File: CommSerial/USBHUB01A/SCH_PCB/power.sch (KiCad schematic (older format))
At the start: 16 parts, among them CON1 PowerIn +5V, J18 JUMP_3X2, SW1 SPST, U3 TPS7A4533KTTR, U4 TPS74801RGWR

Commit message: Vyhozený vypínač, přidaný "Distribution Load Switch"
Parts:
- removed J18: JUMP_3X2, Mlab_Pin_Headers:Straight_2x03, symbol JUMP_3X2
- removed SW1: SPST, Mlab_SW:Prepinaci_3A_SL19121, symbol SPST
- added C1: 10uF, Mlab_R:SMD-0805, symbol C
- added C3: 100nF, Mlab_R:SMD-0603, symbol C
- added D7: LED, Mlab_D:LED_1206, symbol LED
- added R41: 10k, Mlab_R:SMD-0603, symbol R
- added R42: 470R, Mlab_R:SMD-0603, symbol R
- added U9: AP22811, Housings_SSOP:MSOP-8_3x3mm_Pitch0.65mm, symbol AP22811
- C35: value 10uF -> 1uF
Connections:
- net labels added: USB_VBUS_UP
- wire segments 45 -> 61
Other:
- moved on the sheet: C35, C36, C37, C38, C39, C40, D1, R23, R24, R25, R26, U3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

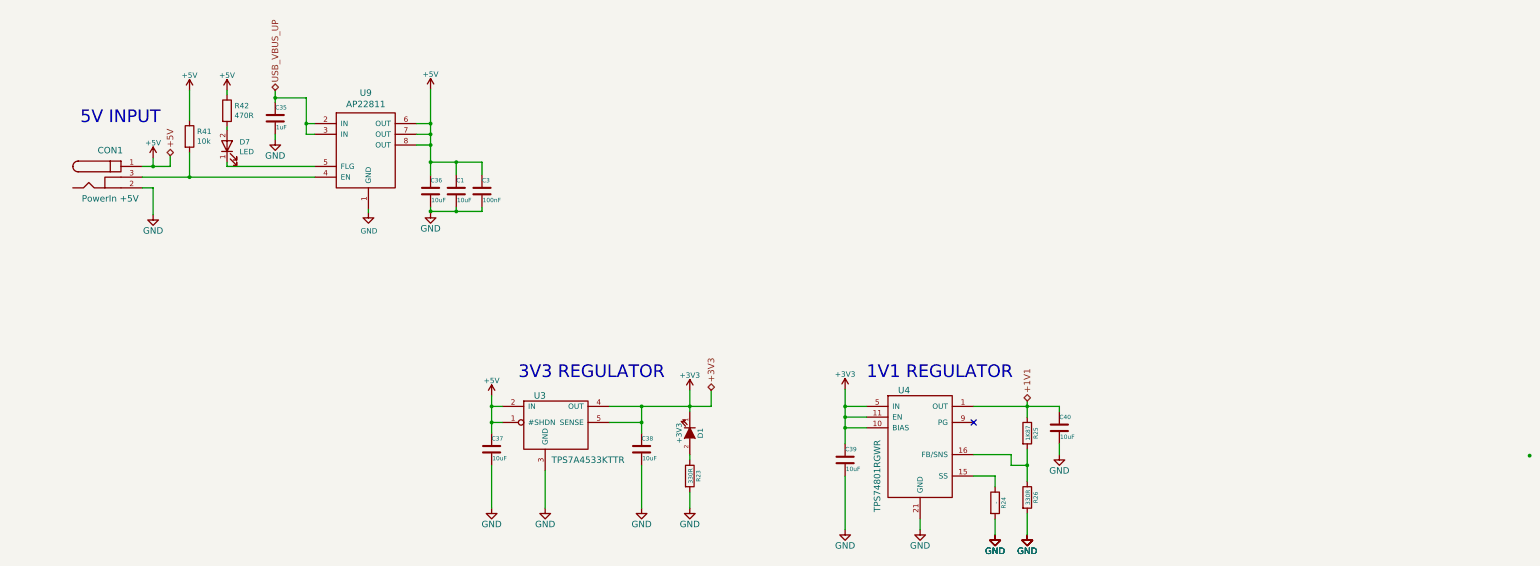
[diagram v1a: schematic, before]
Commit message: Přidání tantalového kondenzátoru na +5V větev
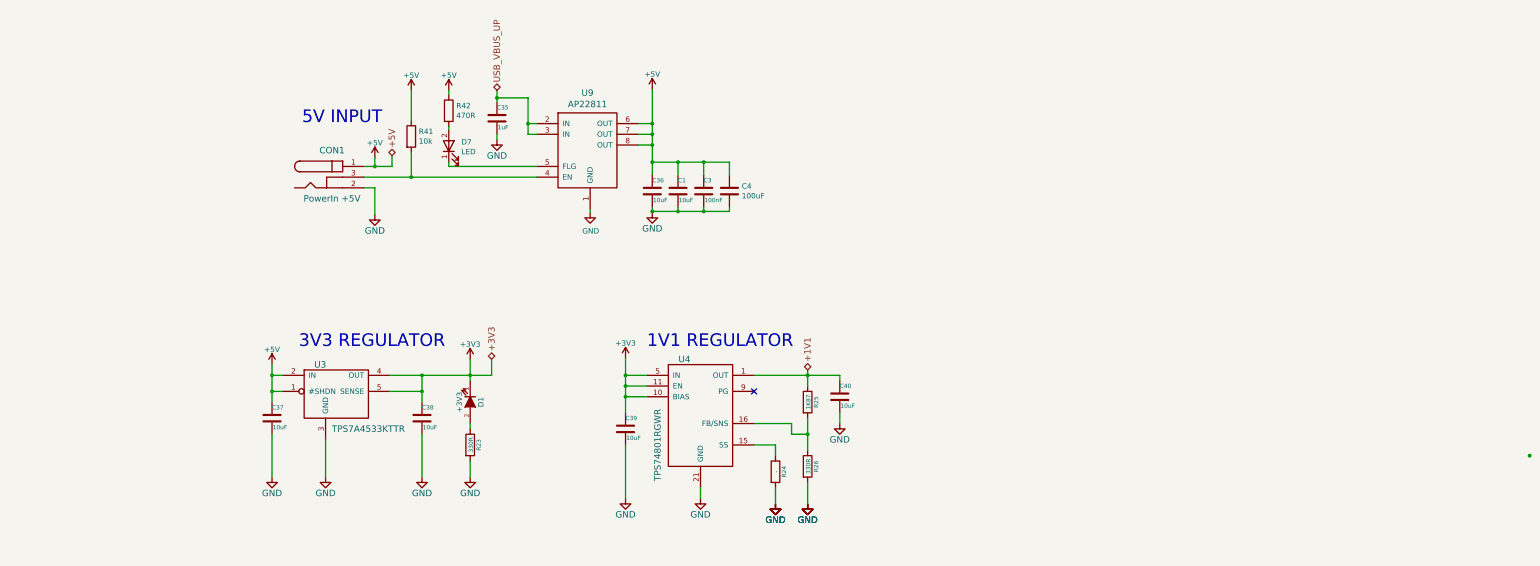
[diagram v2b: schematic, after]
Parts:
- added C4: 100uF, Mlab_C:TantalC_SizeD_Reflow, symbol C
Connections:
- net +5V: now also C4.1
- net GND: now also C4.2
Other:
- moved on the sheet: C1, C3, C35, C36, C37, C38, C39, C40, CON1, D1, D7, R23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

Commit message: USB-Hub-funkcni finalni verze
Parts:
- R25: value 1K87 -> 1K8
- R26: value 330R -> 4k7
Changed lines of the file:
@@
 P 8410 5000
 F 0 "R25" V 8490 5000 40  0000 C CNN
-F 1 "1K87" V 8417 5001 40  0000 C CNN
+F 1 "1K8" V 8417 5001 40  0000 C CNN
 F 2 "Mlab_R:SMD-0603" V 8340 5000 30  0001 C CNN
 F 3 "" H 8410 5000 30  0000 C CNN
@@
 P 8410 5600
 F 0 "R26" V 8490 5600 40  0000 C CNN
-F 1 "330R" V 8417 5601 40  0000 C CNN
+F 1 "4k7" V 8417 5601 40  0000 C CNN
 F 2 "Mlab_R:SMD-0603" V 8340 5600 30  0001 C CNN
 F 3 "" H 8410 5600 30  0000 C CNN
